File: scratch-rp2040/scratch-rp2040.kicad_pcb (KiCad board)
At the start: 2 copper layers, 26 parts, among them P1 USB_C_Plug_USB2.0, SW1 SW_SPST, U1 RP2040, U2 NCP1117-3.3_SOT223, U3 W25Q128JVS, Y1 12.000MHz

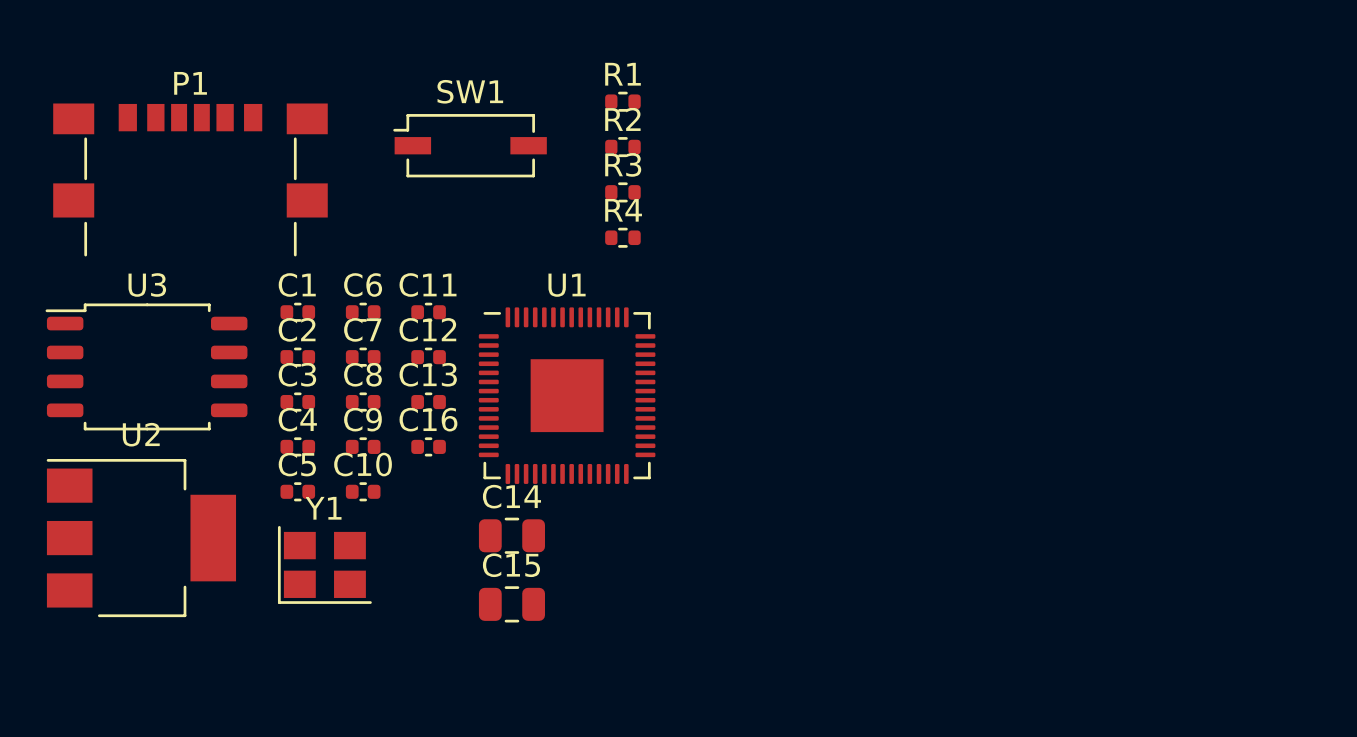
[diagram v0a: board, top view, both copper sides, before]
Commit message: categorized footprints
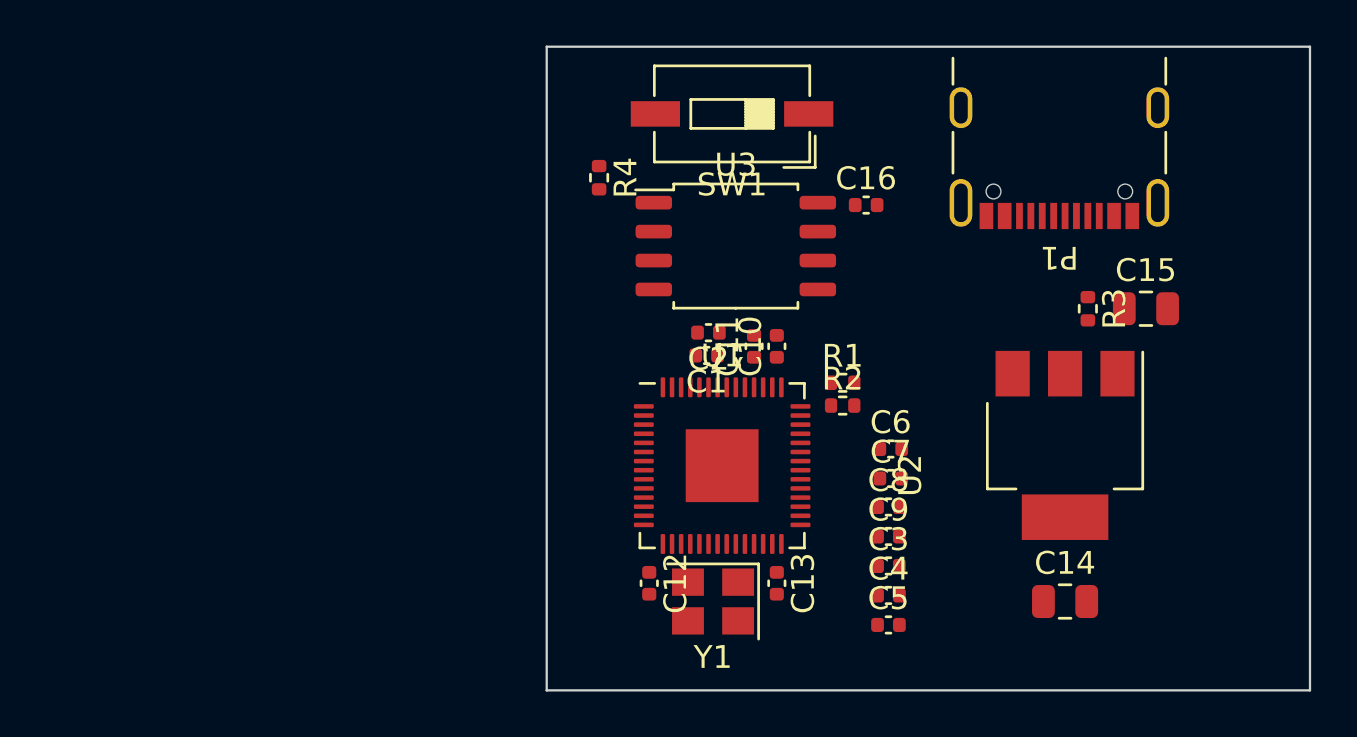
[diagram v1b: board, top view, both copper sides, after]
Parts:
- P1: footprint Connector_USB:USB_C_Receptacle_GCT_USB4135-GF-A_6P_TopMnt_Horizontal -> Connector_USB:USB_C_Receptacle_GCT_USB4105-xx-A_16P_TopMnt_Horizontal
- SW1: footprint Button_Switch_SMD:SW_DIP_SPSTx01_Slide_Copal_CHS-01A_W5.08mm_P1.27mm_JPin -> Button_Switch_SMD:SW_DIP_SPSTx01_Slide_6.7x4.1mm_W6.73mm_P2.54mm_LowProfile_JPin
- moved U2 40.7 mm to (121.2, 65.8), turned to -90 degrees
- moved P1 38.2 mm to (121.0, 52.0), turned to 180 degrees
- moved C15 30.7 mm to (124.8, 59.8)
- moved C3 26.9 mm to (113.5, 71.0)
- moved C4 26.7 mm to (113.5, 72.3)
- moved C5 26.6 mm to (113.5, 73.6)
- moved U3 26.4 mm to (106.8, 57.0)
- moved C14 24.4 mm to (121.2, 72.6)
- moved C6 23.9 mm to (113.6, 65.9)
- moved C7 23.8 mm to (113.6, 67.2)
- moved C8 23.5 mm to (113.5, 68.5)
- moved C9 23.4 mm to (113.5, 69.7)
- moved C16 21.9 mm to (112.5, 55.2)
- moved R3 21.0 mm to (122.2, 59.8), turned to -90 degrees
- moved C10 19.2 mm to (108.6, 61.4), turned to 90 degrees
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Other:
- board outline added: 33.5 x 28.2 mm

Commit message: wiring completed
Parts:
- moved C6 5.60 mm to (113.5, 71.5), turned to 180 degrees
- moved C7 5.30 mm to (113.5, 72.5), turned to 180 degrees
- moved C8 5.05 mm to (113.5, 73.5), turned to 180 degrees
- moved C9 2.65 mm to (111.5, 71.5)
- moved C3 2.46 mm to (111.5, 72.5)
- moved R1 2.37 mm to (112.2, 65.2)
- moved C4 2.30 mm to (111.5, 73.5)
- moved C5 2.16 mm to (111.5, 74.5)
- moved R3 1.60 mm to (121.2, 58.5)
- moved C16 1.29 mm to (112.0, 54.0), turned to 90 degrees
- moved C2 1.01 mm to (106.5, 61.2), turned to 90 degrees
- moved R2 0.75 mm to (112.2, 64.0)
- moved C15 0.56 mm to (124.3, 59.5)
- moved C1 0.55 mm to (105.5, 61.2), turned to 90 degrees
- moved R4 0.45 mm to (101.2, 54.0)
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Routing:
- net GND: track 0.00 -> 100.6 mm, vias 0 -> 6
- net +3.3V: track 0.00 -> 39.5 mm
- net USB_D+: track 0.00 -> 14.8 mm
- net Net-(U1-QSPI_SD3): track 0.00 -> 14.6 mm
- net Net-(U1-QSPI_SCLK): track 0.00 -> 13.7 mm
- net USB_D-: track 0.00 -> 13.4 mm
- net Net-(U1-QSPI_SS): track 0.00 -> 11.7 mm
- net VBUS: track 0.00 -> 10.4 mm
- net Net-(U1-QSPI_SD0): track 0.00 -> 9.59 mm
- net Net-(U1-QSPI_SD1): track 0.00 -> 8.22 mm
- net Net-(U1-QSPI_SD2): track 0.00 -> 6.90 mm
- net Net-(U1-USB_DP): track 0.00 -> 5.88 mm, vias 0 -> 2
- net Net-(U1-USB_DM): track 0.00 -> 4.97 mm, vias 0 -> 2
- net Net-(U1-XIN): track 0.00 -> 3.97 mm
- net Net-(U1-XOUT): track 0.00 -> 3.93 mm
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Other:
- board size 33.5 x 28.2 mm -> 44.2 x 28.2 mm

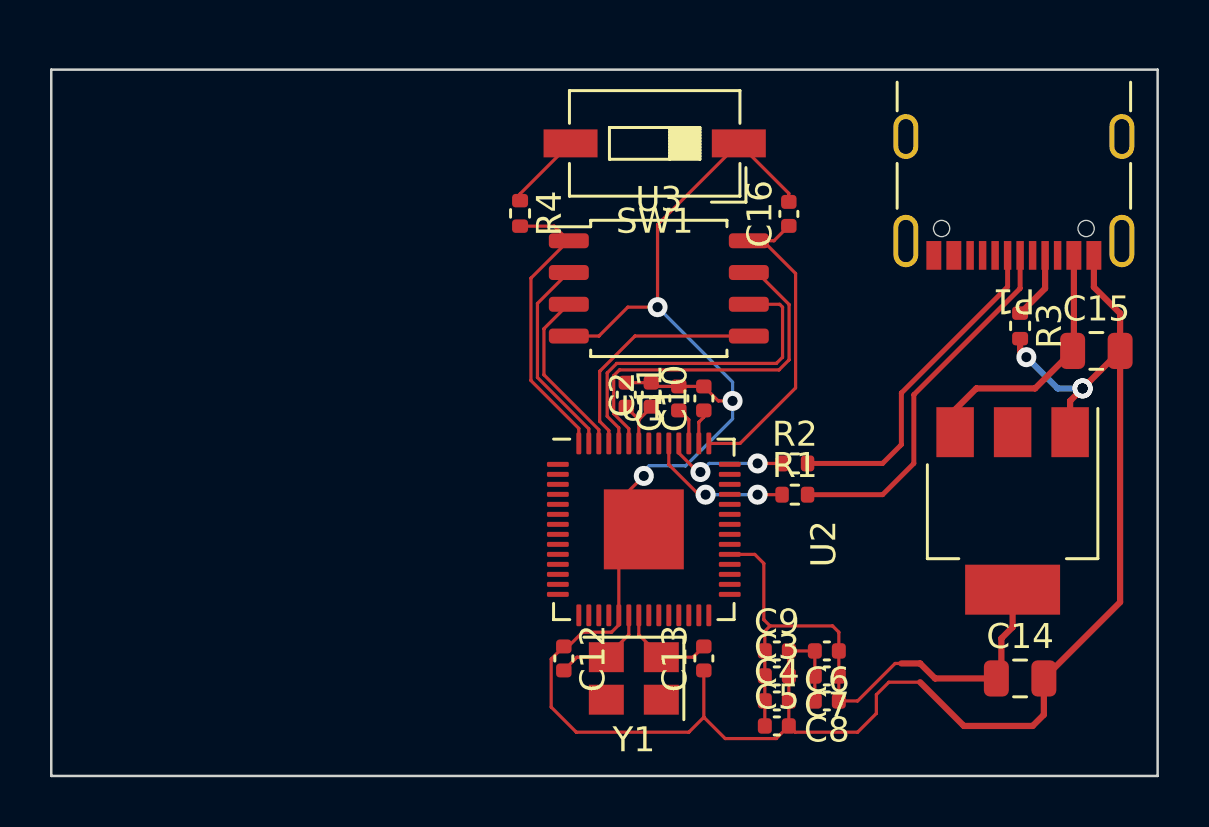
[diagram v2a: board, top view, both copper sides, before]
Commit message: pcb wiring including switches
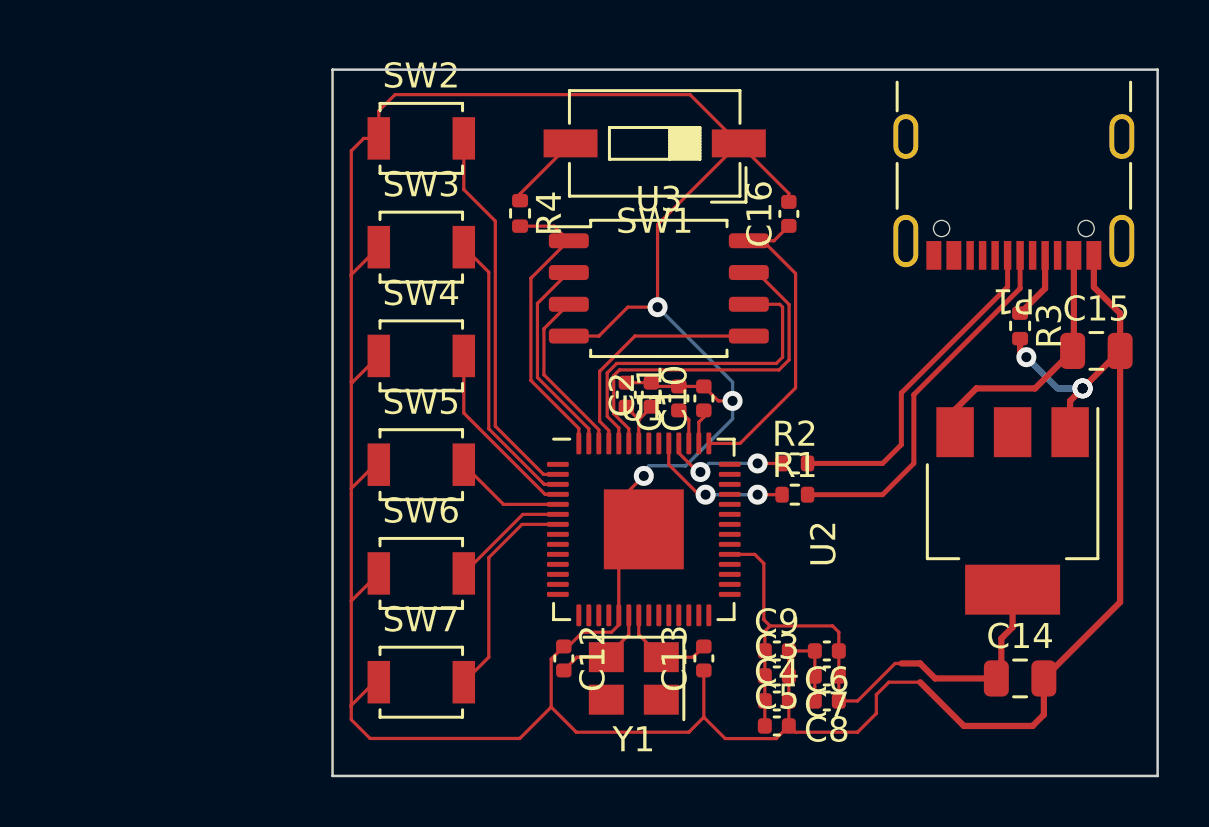
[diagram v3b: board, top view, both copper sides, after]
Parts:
- added SW2: SW_SPST, Button_Switch_SMD:SW_SPST_B3U-1000P, F.Cu at (97.3, 51.0)
- added SW3: SW_SPST, Button_Switch_SMD:SW_SPST_B3U-1000P, F.Cu at (97.3, 55.4)
- added SW4: SW_SPST, Button_Switch_SMD:SW_SPST_B3U-1000P, F.Cu at (97.3, 59.7)
- added SW5: SW_SPST, Button_Switch_SMD:SW_SPST_B3U-1000P, F.Cu at (97.3, 64.0)
- added SW6: SW_SPST, Button_Switch_SMD:SW_SPST_B3U-1000P, F.Cu at (97.3, 68.4)
- added SW7: SW_SPST, Button_Switch_SMD:SW_SPST_B3U-1000P, F.Cu at (97.3, 72.8)
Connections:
- U1 pad 2: unconnected-(U1-GPIO0-Pad2) -> Net-(SW2-B)
- U1 pad 3: unconnected-(U1-GPIO1-Pad3) -> Net-(SW3-B)
- U1 pad 4: unconnected-(U1-GPIO2-Pad4) -> Net-(SW4-B)
- U1 pad 5: unconnected-(U1-GPIO3-Pad5) -> Net-(SW5-B)
- U1 pad 6: unconnected-(U1-GPIO4-Pad6) -> Net-(SW6-B)
- U1 pad 7: unconnected-(U1-GPIO5-Pad7) -> Net-(SW7-B)
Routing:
- net GND: track 100.6 -> 157.8 mm
- net Net-(SW2-B): track 0.00 -> 15.3 mm
- net Net-(SW3-B): track 0.00 -> 11.4 mm
- net Net-(SW7-B): track 0.00 -> 8.71 mm
- net Net-(SW4-B): track 0.00 -> 7.39 mm
- net Net-(SW6-B): track 0.00 -> 4.74 mm
- net Net-(SW5-B): track 0.00 -> 4.42 mm
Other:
- board size 44.2 x 28.2 mm -> 33 x 28.2 mm

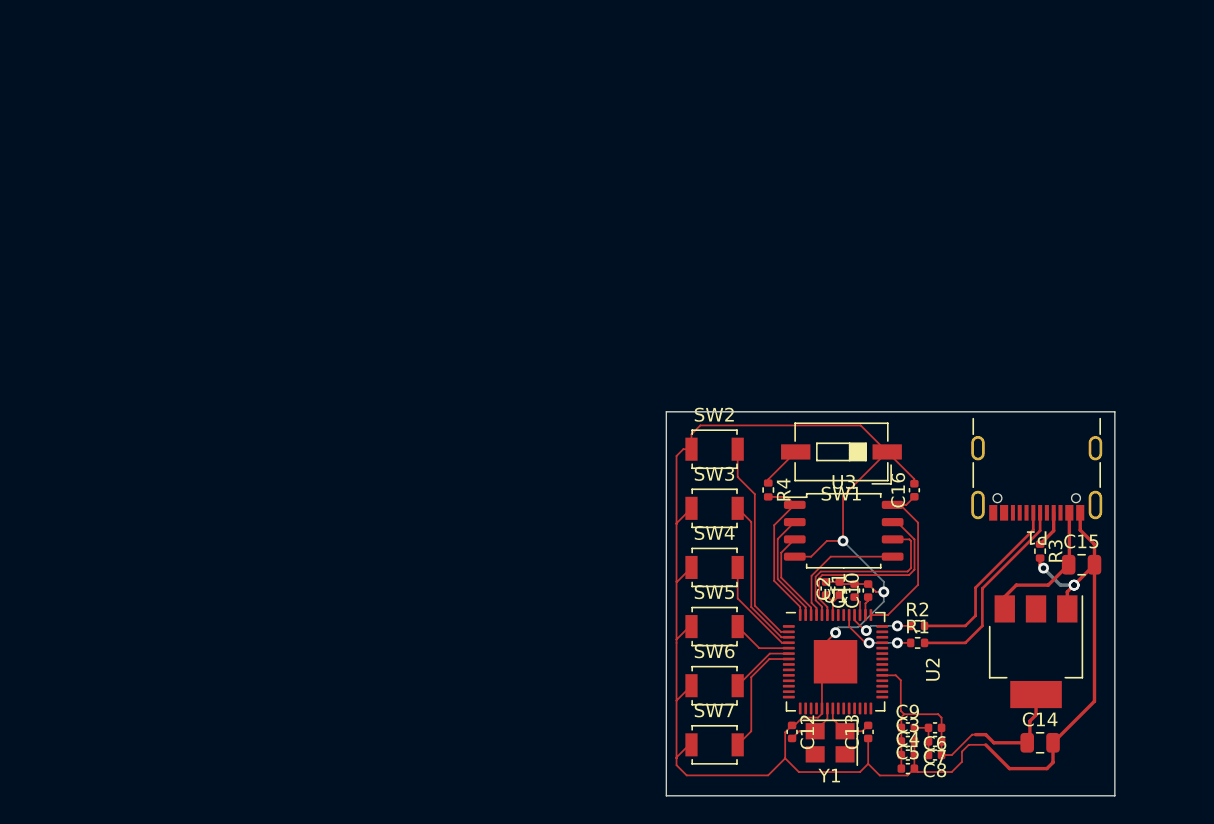
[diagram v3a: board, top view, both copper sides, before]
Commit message: usb receptacle changed
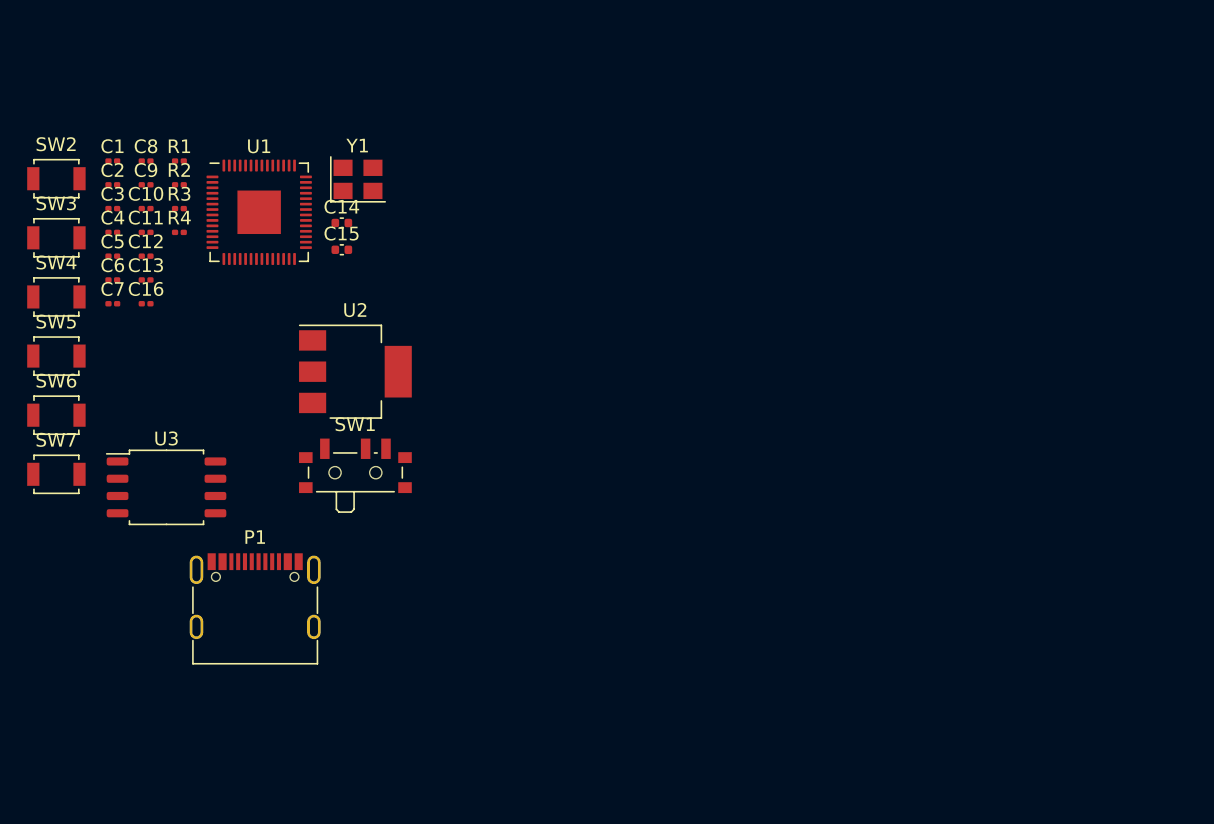
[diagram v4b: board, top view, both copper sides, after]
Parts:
- C1, C10, C11, C12, C13, C16, C2, C3, C4, C5, C6, C7, C8, C9: footprint Capacitor_SMD:C_0402_1005Metric -> Capacitor_SMD:C_0201_0603Metric
- C14, C15: footprint Capacitor_SMD:C_0805_2012Metric -> Capacitor_SMD:C_0402_1005Metric
- P1: footprint Connector_USB:USB_C_Receptacle_GCT_USB4105-xx-A_16P_TopMnt_Horizontal -> Connector_USB:USB_C_Receptacle_G-Switch_GT-USB-7010ASV
- R1, R2, R3, R4: footprint Resistor_SMD:R_0402_1005Metric -> Resistor_SMD:R_0201_0603Metric
- SW1: footprint Button_Switch_SMD:SW_DIP_SPSTx01_Slide_6.7x4.1mm_W6.73mm_P2.54mm_LowProfile_JPin -> Button_Switch_SMD:SW_SPDT_PCM12
- Y1: value 12.000MHz -> 12MHz
- moved C8 72.7 mm to (55.5, 29.8), turned to 0 degrees
- moved C3 70.4 mm to (53.0, 33.3)
- moved C4 70.0 mm to (53.0, 35.0)
- moved C5 69.6 mm to (53.0, 36.8)
- moved C6 68.9 mm to (53.0, 38.5), turned to 0 degrees
- moved C9 68.8 mm to (55.5, 31.5)
- moved C7 68.5 mm to (53.0, 40.3), turned to 0 degrees
- moved R3 68.2 mm to (57.9, 33.3), turned to 0 degrees
- moved R1 64.9 mm to (57.9, 29.8)
- moved C14 64.0 mm to (69.9, 34.4)
- moved R2 63.3 mm to (57.9, 31.5)
- moved C13 62.7 mm to (55.5, 38.5), turned to 0 degrees
- moved C1 61.2 mm to (53.0, 29.8), turned to 0 degrees
- moved C2 61.2 mm to (53.0, 31.5), turned to 0 degrees
- moved C10 60.1 mm to (55.5, 33.3), turned to 0 degrees
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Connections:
- Y1 pad 2: Net-(U1-XIN) -> GND
- Y1 pad 3: (no net) -> Net-(U1-XIN)
- Y1 pad 4: (no net) -> GND
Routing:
- net GND: track 157.8 -> 0.00 mm, vias 6 -> 0
- net +3.3V: track 39.5 -> 0.00 mm
- net Net-(SW2-B): track 15.3 -> 0.00 mm
- net USB_D+: track 14.8 -> 0.00 mm
- net Net-(U1-QSPI_SD3): track 14.6 -> 0.00 mm
- net Net-(U1-QSPI_SCLK): track 13.7 -> 0.00 mm
- net USB_D-: track 13.4 -> 0.00 mm
- net Net-(U1-QSPI_SS): track 11.7 -> 0.00 mm
- net Net-(SW3-B): track 11.4 -> 0.00 mm
- net VBUS: track 10.4 -> 0.00 mm
- net Net-(U1-QSPI_SD0): track 9.59 -> 0.00 mm
- net Net-(SW7-B): track 8.71 -> 0.00 mm
- net Net-(U1-QSPI_SD1): track 8.22 -> 0.00 mm
- net Net-(SW4-B): track 7.39 -> 0.00 mm
- net Net-(U1-QSPI_SD2): track 6.90 -> 0.00 mm
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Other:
- board outline removed

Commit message: parts placed
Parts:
- moved SW2 34.2 mm to (81.0, 42.7), turned to 90 degrees
- moved SW5 32.8 mm to (81.0, 37.6), turned to -90 degrees
- moved SW6 30.6 mm to (77.5, 37.6), turned to -90 degrees
- moved SW3 29.5 mm to (77.5, 42.7), turned to 90 degrees
- moved SW7 29.3 mm to (73.9, 37.6), turned to -90 degrees
- moved SW4 25.2 mm to (73.9, 42.7), turned to 90 degrees
- moved U3 21.8 mm to (78.0, 48.0), turned to 180 degrees
- moved R1 18.3 mm to (67.6, 45.3), turned to -90 degrees
- moved P1 16.5 mm to (58.2, 47.4)
- moved R2 16.4 mm to (66.9, 45.3), turned to -90 degrees
- moved U2 16.1 mm to (57.1, 36.8), turned to 90 degrees
- moved C10 15.5 mm to (65.4, 45.3), turned to -90 degrees
- moved R4 15.4 mm to (69.1, 45.7)
- moved C12 15.2 mm to (70.4, 34.4), turned to 90 degrees
- moved C11 14.8 mm to (66.1, 45.3), turned to -90 degrees
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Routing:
- net Net-(U1-XIN): track 0.00 -> 6.24 mm
- net GND: track 0.00 -> 4.00 mm
- net Net-(U1-XOUT): track 0.00 -> 2.43 mm

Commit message: parts placement considering...
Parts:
- moved SW1 13.9 mm to (82.1, 47.3), turned to 90 degrees
- moved C8 8.68 mm to (60.5, 41.3), turned to -90 degrees
- moved SW2 8.64 mm to (80.2, 34.1), turned to 180 degrees
- moved C7 8.42 mm to (54.7, 41.3), turned to -90 degrees
- moved C9 8.19 mm to (59.5, 41.3), turned to -90 degrees
- moved C6 8.01 mm to (55.7, 41.3), turned to -90 degrees
- moved C3 7.86 mm to (58.6, 41.3), turned to -90 degrees
- moved C5 7.77 mm to (56.6, 41.3), turned to -90 degrees
- moved C4 7.72 mm to (57.6, 41.3), turned to -90 degrees
- moved R4 6.93 mm to (75.8, 44.2), turned to 90 degrees
- moved SW5 6.67 mm to (75.4, 34.1), turned to 0 degrees
- moved SW4 6.52 mm to (80.2, 40.8), turned to 180 degrees
- moved SW3 5.88 mm to (80.2, 37.4), turned to 180 degrees
- moved U3 4.64 mm to (73.4, 49.0)
- moved SW7 3.52 mm to (75.4, 40.8), turned to 0 degrees
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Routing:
- net Net-(U1-XIN): track 6.24 -> 0.00 mm
- net GND: track 4.00 -> 0.00 mm
- net +1V1: track 0.00 -> 3.29 mm, vias 0 -> 1
- net Net-(U1-XOUT): track 2.43 -> 0.00 mm

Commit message: wiring finished
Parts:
- moved SW1 14.3 mm to (68.0, 49.6), turned to 0 degrees
- moved SW2 8.97 mm to (76.8, 42.4), turned to 0 degrees
- moved R4 8.15 mm to (68.0, 46.4)
- moved SW6 6.94 mm to (81.6, 34.4), turned to 180 degrees
- moved C7 6.59 mm to (61.3, 40.6), turned to 0 degrees
- moved SW7 6.56 mm to (76.8, 34.4)
- moved C8 6.45 mm to (61.3, 34.9), turned to 0 degrees
- moved C6 5.82 mm to (61.3, 39.7), turned to 0 degrees
- moved U3 5.76 mm to (79.2, 48.8)
- moved C9 5.72 mm to (61.3, 35.8), turned to 0 degrees
- moved C5 5.30 mm to (61.3, 38.7), turned to 0 degrees
- moved C3 5.24 mm to (61.3, 36.8), turned to 0 degrees
- moved SW3 5.16 mm to (81.6, 42.4)
- moved C4 5.09 mm to (61.3, 37.8), turned to 0 degrees
- moved SW5 4.55 mm to (76.8, 38.4)
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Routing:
- net GND: track 0.00 -> 118.4 mm, vias 0 -> 6
- net +3.3V: track 0.00 -> 78.7 mm, vias 0 -> 7
- net Net-(U1-QSPI_SS): track 0.00 -> 22.9 mm, vias 0 -> 2
- net Net-(U1-QSPI_SD1): track 0.00 -> 15.0 mm, vias 0 -> 2
- net Net-(U1-QSPI_SD2): track 0.00 -> 14.9 mm, vias 0 -> 2
- net +1V1: track 3.29 -> 17.8 mm, vias 1 -> 2
- net Net-(SW6-B): track 0.00 -> 11.6 mm
- net USB_D+: track 0.00 -> 11.4 mm
- net Net-(SW7-B): track 0.00 -> 10.5 mm
- net Net-(SW4-B): track 0.00 -> 10.2 mm
- net USB_D-: track 0.00 -> 9.66 mm
- net Net-(SW3-B): track 0.00 -> 9.48 mm
- net Net-(U1-QSPI_SD3): track 0.00 -> 9.36 mm
- net Net-(SW5-B): track 0.00 -> 9.20 mm
- net Net-(U1-QSPI_SCLK): track 0.00 -> 8.44 mm
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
